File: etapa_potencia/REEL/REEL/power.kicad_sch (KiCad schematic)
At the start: 20 parts

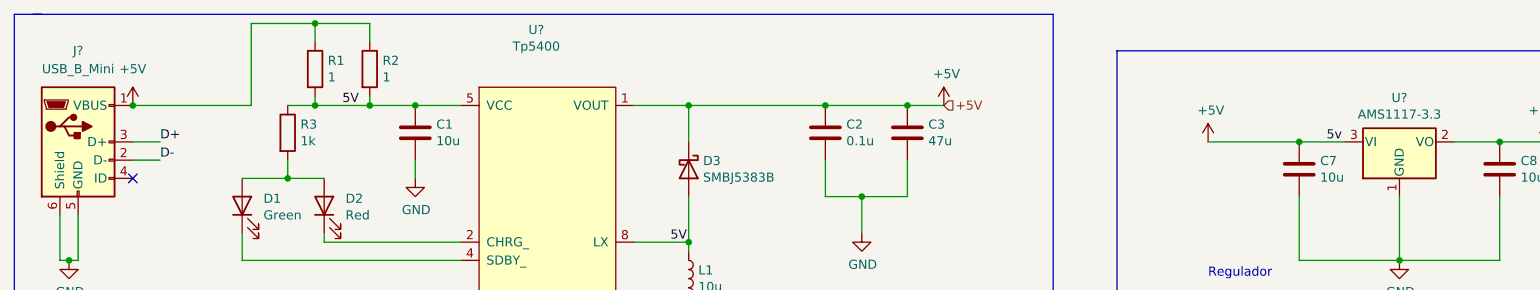
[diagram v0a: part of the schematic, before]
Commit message: Conexiones corregidas, PCB ordenada
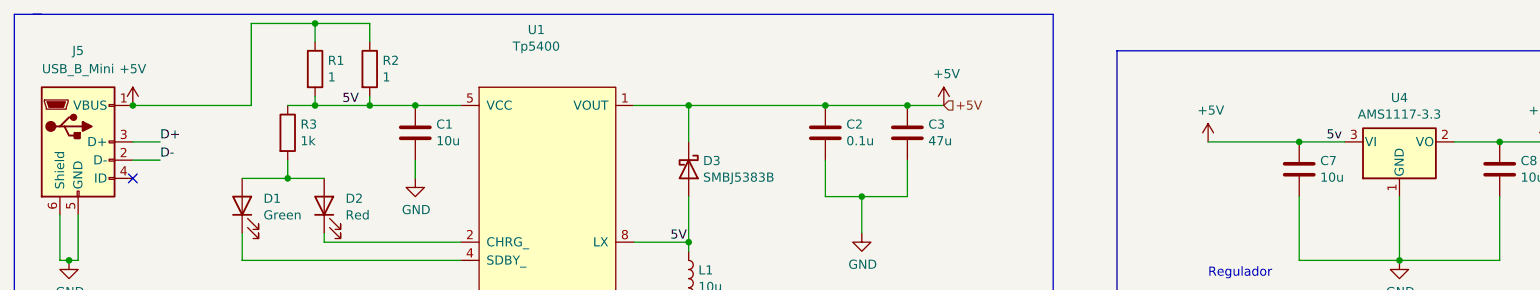
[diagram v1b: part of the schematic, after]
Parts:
- gave numbers to parts that had none: 3
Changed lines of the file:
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@@
   (symbol (lib_id "power:GND") (at 170.18 91.44 0) (unit 1)
     (in_bom yes) (on_board yes)
-    (property "Reference" "#PWR?" (id 0) (at 170.18 97.79 0)
+    (property "Reference" "#PWR024" (id 0) (at 170.18 97.79 0)
       (effects (font (size 1.27 1.27)) hide)
     )
@@
   (symbol (lib_id "Connector:USB_B_Mini") (at 60.96 78.74 0) (unit 1)
     (in_bom yes) (on_board yes) (fields_autoplaced)
-    (property "Reference" "J?" (id 0) (at 60.96 66.04 0))
+    (property "Reference" "J5" (id 0) (at 60.96 66.04 0))
     (property "Value" "USB_B_Mini" (id 1) (at 60.96 68.58 0))
     (property "Footprint" "Connector_USB:USB_Mini-B_AdamTech_MUSB-B5-S-VT-TSMT-1_SMD_Vertical" (id 2) (at 64.77 80.01 0)
@@
   (symbol (lib_id "power:GND") (at 245.11 95.25 0) (unit 1)
     (in_bom yes) (on_board yes)
-    (property "Reference" "#PWR?" (id 0) (at 245.11 101.6 0)
+    (property "Reference" "#PWR027" (id 0) (at 245.11 101.6 0)
       (effects (font (size 1.27 1.27)) hide)
     )
@@
   (symbol (lib_id "TP5400:Tp5400") (at 127 87.63 0) (unit 1)
     (in_bom yes) (on_board yes)
-    (property "Reference" "U?" (id 0) (at 124.8156 63.119 0))
+    (property "Reference" "U1" (id 0) (at 124.8156 63.119 0))
     (property "Value" "Tp5400" (id 1) (at 124.8156 65.4304 0))
     (property "Footprint" "KiCad:TP5410" (id 2) (at 121.92 68.58 0)
@@
   (symbol (lib_id "power:GND") (at 107.95 83.82 0) (unit 1)
     (in_bom yes) (on_board yes)
-    (property "Reference" "#PWR?" (id 0) (at 107.95 90.17 0)
+    (property "Reference" "#PWR022" (id 0) (at 107.95 90.17 0)
       (effects (font (size 1.27 1.27)) hide)
     )
@@
   (symbol (lib_id "Regulator_Linear:AMS1117-3.3") (at 245.11 78.74 0) (unit 1)
     (in_bom yes) (on_board yes)
-    (property "Reference" "U?" (id 0) (at 245.11 72.5932 0))
+    (property "Reference" "U4" (id 0) (at 245.11 72.5932 0))
     (property "Value" "AMS1117-3.3" (id 1) (at 245.11 74.9046 0))
     (property "Footprint" "Package_TO_SOT_SMD:SOT-223-3_TabPin2" (id 2) (at 245.11 73.66 0)
@@
   (symbol (lib_id "power:+3.3V") (at 265.43 78.74 0) (unit 1)
     (in_bom yes) (on_board yes)
-    (property "Reference" "#PWR?" (id 0) (at 265.43 82.55 0)
+    (property "Reference" "#PWR028" (id 0) (at 265.43 82.55 0)
       (effects (font (size 1.27 1.27)) hide)
     )
@@
   (symbol (lib_id "power:GND") (at 59.69 95.25 0) (unit 1)
     (in_bom yes) (on_board yes)
-    (property "Reference" "#PWR?" (id 0) (at 59.69 101.6 0)
+    (property "Reference" "#PWR020" (id 0) (at 59.69 101.6 0)
       (effects (font (size 1.27 1.27)) hide)
     )
@@
   (symbol (lib_id "power:GND") (at 138.43 129.54 0) (unit 1)
     (in_bom yes) (on_board yes)
-    (property "Reference" "#PWR?" (id 0) (at 138.43 135.89 0)
+    (property "Reference" "#PWR023" (id 0) (at 138.43 135.89 0)
       (effects (font (size 1.27 1.27)) hide)
     )
@@
   (symbol (lib_id "power:+5V") (at 218.44 78.74 0) (unit 1)
     (in_bom yes) (on_board yes)
-    (property "Reference" "#PWR?" (id 0) (at 218.44 82.55 0)
+    (property "Reference" "#PWR026" (id 0) (at 218.44 82.55 0)
       (effects (font (size 1.27 1.27)) hide)
     )
@@
   (symbol (lib_id "power:+5V") (at 181.61 73.66 0) (unit 1)
     (in_bom yes) (on_board yes)
-    (property "Reference" "#PWR?" (id 0) (at 181.61 77.47 0)
+    (property "Reference" "#PWR025" (id 0) (at 181.61 77.47 0)
       (effects (font (size 1.27 1.27)) hide)
     )
@@
   (symbol (lib_id "power:+5V") (at 68.58 73.66 0) (unit 1)
     (in_bom yes) (on_board yes) (fields_autoplaced)
-    (property "Reference" "#PWR?" (id 0) (at 68.58 77.47 0)
-      (effects (font (size 1.27 1.27)) hide)
-    )
+    (property "Reference" "#PWR021" (id 0) (at 68.58 77.47 0)
+      (effects (font (size 1.27 1.27)) hide)
+    )

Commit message: Primera organización huellas
Organización de huellas y conectores, falta parte de potencia
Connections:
- net +5V: no longer J5.1 (VBUS), R1.1, R2.1
- net +3V3 renamed +3.3V
- new net 5V_USB: J5.1 (VBUS), R1.1, R2.1
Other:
- moved on the sheet: C7, C8
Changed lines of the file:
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@@
   (junction (at 93.98 73.66) (diameter 0) (color 0 0 0 0)
-  )
-  (junction (at 68.58 73.66) (diameter 0) (color 0 0 0 0)
   )
   (junction (at 259.08 78.74) (diameter 0) (color 0 0 0 0)
@@
     (stroke (width 0) (type default) (color 0 0 0 0))
   )
-  (wire (pts (xy 231.14 95.25) (xy 231.14 86.36))
+  (wire (pts (xy 231.14 95.25) (xy 231.14 88.9))
     (stroke (width 0) (type default) (color 0 0 0 0))
   )
@@
     (stroke (width 0) (type default) (color 0 0 0 0))
   )
+  (wire (pts (xy 259.08 80.01) (xy 259.08 78.74))
+    (stroke (width 0) (type default) (color 0 0 0 0))
+  )
   (wire (pts (xy 93.98 62.23) (xy 93.98 64.77))
     (stroke (width 0) (type default) (color 0 0 0 0))
@@
     (stroke (width 0) (type default) (color 0 0 0 0))
   )
-  (wire (pts (xy 259.08 86.36) (xy 259.08 95.25))
+  (wire (pts (xy 259.08 87.63) (xy 259.08 95.25))
     (stroke (width 0) (type default) (color 0 0 0 0))
   )
@@
     (stroke (width 0) (type default) (color 0 0 0 0))
   )
+  (wire (pts (xy 231.14 81.28) (xy 231.14 78.74))
+    (stroke (width 0) (type default) (color 0 0 0 0))
+  )
   (wire (pts (xy 85.09 62.23) (xy 93.98 62.23))
     (stroke (width 0) (type default) (color 0 0 0 0))
@@
   )
   (label "5v" (at 234.95 78.74 0)
+    (effects (font (size 1.27 1.27)) (justify left bottom))
+  )
+  (label "5V_USB" (at 74.93 73.66 0)
     (effects (font (size 1.27 1.27)) (justify left bottom))
   )
@@
     (pin "1")
   )
-  (symbol (lib_id "Device:C") (at 231.14 82.55 0) (unit 1)
-    (in_bom yes) (on_board yes)
-    (property "Reference" "C7" (id 0) (at 234.061 81.3816 0)
-      (effects (font (size 1.27 1.27)) (justify left))
-    )
-    (property "Value" "10u" (id 1) (at 234.061 83.693 0)
-      (effects (font (size 1.27 1.27)) (justify left))
-    )
-    (property "Footprint" "Capacitor_SMD:C_1210_3225Metric_Pad1.33x2.70mm_HandSolder" (id 2) (at 232.1052 86.36 0)
-      (effects (font (size 1.27 1.27)) hide)
-    )
-    (property "Datasheet" "~" (id 3) (at 231.14 82.55 0)
+  (symbol (lib_id "Device:C") (at 231.14 85.09 0) (unit 1)
+    (in_bom yes) (on_board yes)
+    (property "Reference" "C7" (id 0) (at 234.061 83.9216 0)
+      (effects (font (size 1.27 1.27)) (justify left))
+    )
+    (property "Value" "10u" (id 1) (at 234.061 86.233 0)
+      (effects (font (size 1.27 1.27)) (justify left))
+    )
+    (property "Footprint" "Capacitor_SMD:C_1210_3225Metric_Pad1.33x2.70mm_HandSolder" (id 2) (at 232.1052 88.9 0)
+      (effects (font (size 1.27 1.27)) hide)
+    )
+    (property "Datasheet" "~" (id 3) (at 231.14 85.09 0)
       (effects (font (size 1.27 1.27)) hide)
     )
@@
     (pin "3")
   )
-  (symbol (lib_id "power:+3.3V") (at 265.43 78.74 0) (unit 1)
-    (in_bom yes) (on_board yes)
-    (property "Reference" "#PWR028" (id 0) (at 265.43 82.55 0)
-      (effects (font (size 1.27 1.27)) hide)
-    )
-    (property "Value" "+3.3V" (id 1) (at 265.811 74.3458 0))
-    (property "Footprint" "" (id 2) (at 265.43 78.74 0)
-      (effects (font (size 1.27 1.27)) hide)
-    )
-    (property "Datasheet" "" (id 3) (at 265.43 78.74 0)
-      (effects (font (size 1.27 1.27)) hide)
-    )
-    (pin "1")
-  )
   (symbol (lib_id "Device:LED") (at 95.25 87.63 90) (unit 1)
     (in_bom yes) (on_board yes)
@@
     (pin "2")
   )
-  (symbol (lib_id "Device:C") (at 259.08 82.55 0) (unit 1)
-    (in_bom yes) (on_board yes)
-    (property "Reference" "C8" (id 0) (at 262.001 81.3816 0)
-      (effects (font (size 1.27 1.27)) (justify left))
-    )
-    (property "Value" "10u" (id 1) (at 262.001 83.693 0)
-      (effects (font (size 1.27 1.27)) (justify left))
-    )
-    (property "Footprint" "Capacitor_SMD:C_1210_3225Metric_Pad1.33x2.70mm_HandSolder" (id 2) (at 260.0452 86.36 0)
-      (effects (font (size 1.27 1.27)) hide)
-    )
-    (property "Datasheet" "~" (id 3) (at 259.08 82.55 0)
+  (symbol (lib_id "Device:C") (at 259.08 83.82 0) (unit 1)
+    (in_bom yes) (on_board yes)
+    (property "Reference" "C8" (id 0) (at 262.001 82.6516 0)
+      (effects (font (size 1.27 1.27)) (justify left))
+    )
+    (property "Value" "10u" (id 1) (at 262.001 84.963 0)
+      (effects (font (size 1.27 1.27)) (justify left))
+    )
+    (property "Footprint" "Capacitor_SMD:C_1210_3225Metric_Pad1.33x2.70mm_HandSolder" (id 2) (at 260.0452 87.63 0)
+      (effects (font (size 1.27 1.27)) hide)
+    )
+    (property "Datasheet" "~" (id 3) (at 259.08 83.82 0)
       (effects (font (size 1.27 1.27)) hide)
     )
@@
     (pin "2")
   )
-  (symbol (lib_id "power:+5V") (at 181.61 73.66 0) (unit 1)
-    (in_bom yes) (on_board yes)
-    (property "Reference" "#PWR025" (id 0) (at 181.61 77.47 0)
-      (effects (font (size 1.27 1.27)) hide)
-    )
-    (property "Value" "+5V" (id 1) (at 181.991 69.2658 0))
-    (property "Footprint" "" (id 2) (at 181.61 73.66 0)
-      (effects (font (size 1.27 1.27)) hide)
-    )
-    (property "Datasheet" "" (id 3) (at 181.61 73.66 0)
-      (effects (font (size 1.27 1.27)) hide)
-    )
-    (pin "1")
-  )
-  (symbol (lib_id "power:+5V") (at 68.58 73.66 0) (unit 1)
-    (in_bom yes) (on_board yes) (fields_autoplaced)
-    (property "Reference" "#PWR021" (id 0) (at 68.58 77.47 0)
-      (effects (font (size 1.27 1.27)) hide)
-    )
-    (property "Value" "+5V" (id 1) (at 68.58 68.58 0))
-    (property "Footprint" "" (id 2) (at 68.58 73.66 0)
-      (effects (font (size 1.27 1.27)) hide)
-    )
-    (property "Datasheet" "" (id 3) (at 68.58 73.66 0)
-      (effects (font (size 1.27 1.27)) hide)
-    )
-    (pin "1")
-  )
   (symbol (lib_id "Device:C") (at 165.1 77.47 0) (unit 1)

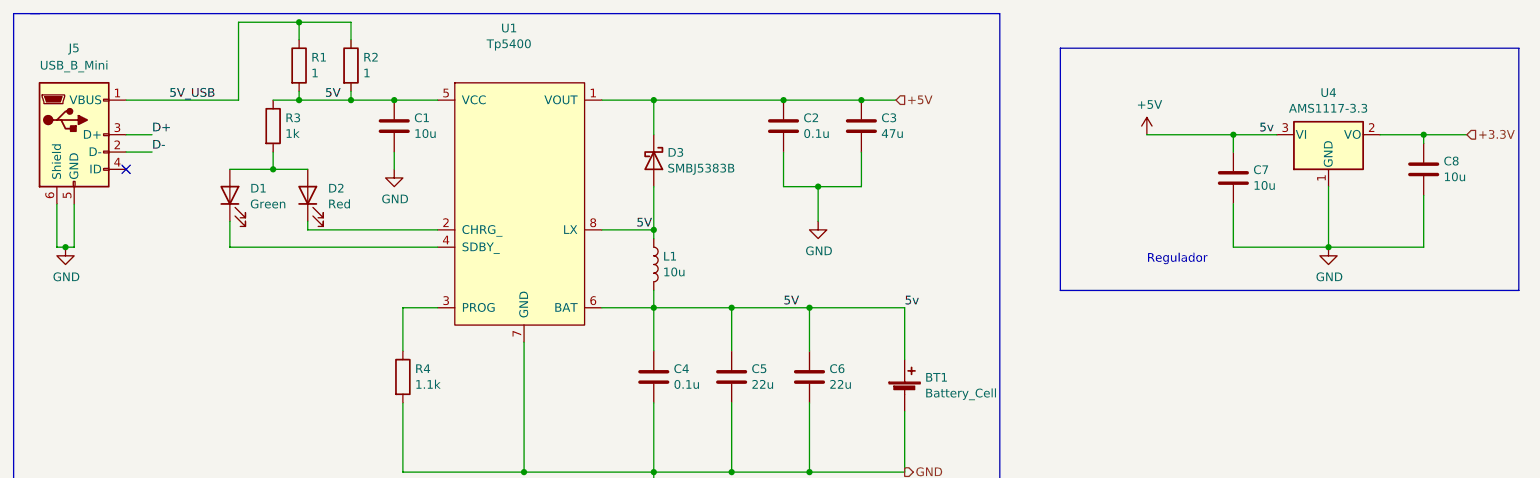
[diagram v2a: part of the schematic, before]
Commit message: Cambios en diagrama, separacion tierras, y capacitores
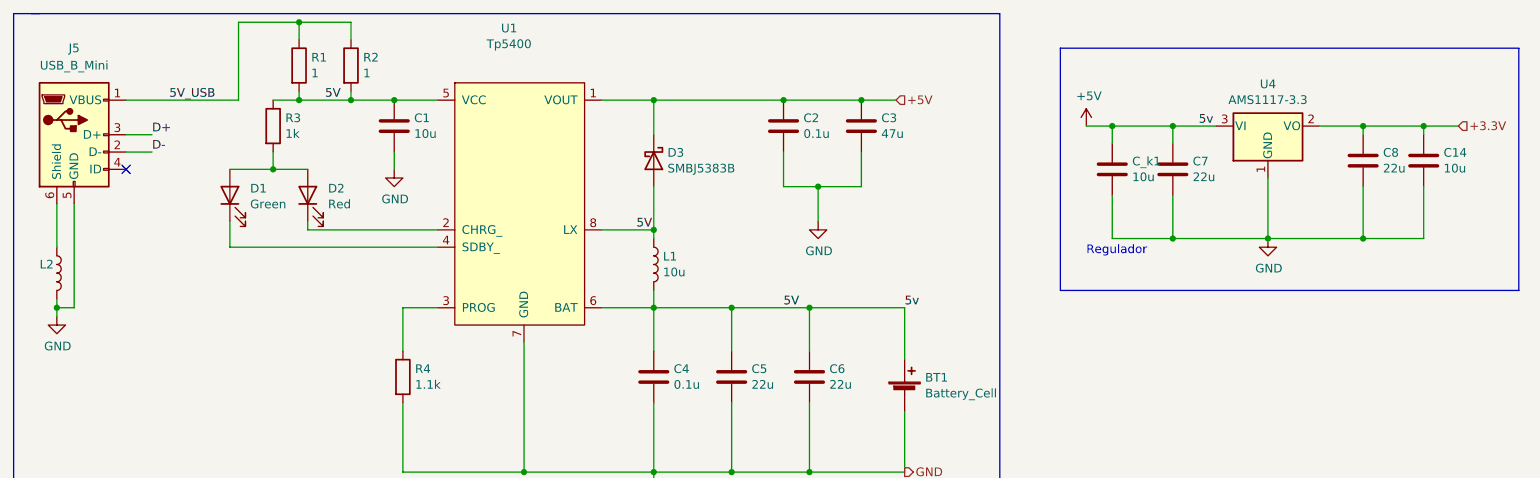
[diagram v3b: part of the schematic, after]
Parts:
- added C14, C_k1: 10u, Capacitor_SMD:C_1210_3225Metric_Pad1.33x2.70mm_HandSolder, symbol Device:C
- added L2: (no value), Inductor_SMD:L_6.3x6.3_H3, symbol Device:L
- BT1: footprint Battery:BatteryHolder_Bulgin_BX0036_1xC -> Connector_JST:JST_PH_B2B-PH-K_1x02_P2.00mm_Vertical
- C7, C8: value 10u -> 22u
- L1: footprint Inductor_SMD:L_0805_2012Metric_Pad1.05x1.20mm_HandSolder -> Inductor_SMD:L_6.3x6.3_H3
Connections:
- net +3.3V: now also C14.1
- net +5V: now also C_k1.1
- net GND: now also C14.2, C_k1.2, L2.2; no longer J5.6 (Shield)
- new net: J5.6 (Shield), L2.1
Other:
- moved on the sheet: C7, C8, U4

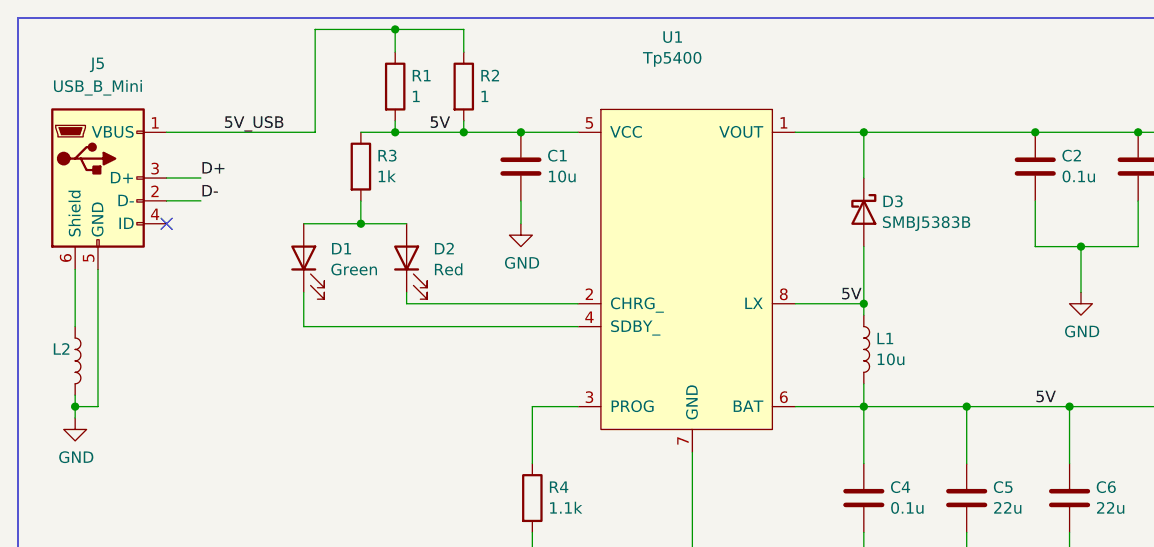
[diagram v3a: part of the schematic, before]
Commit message: modificaciones por caras
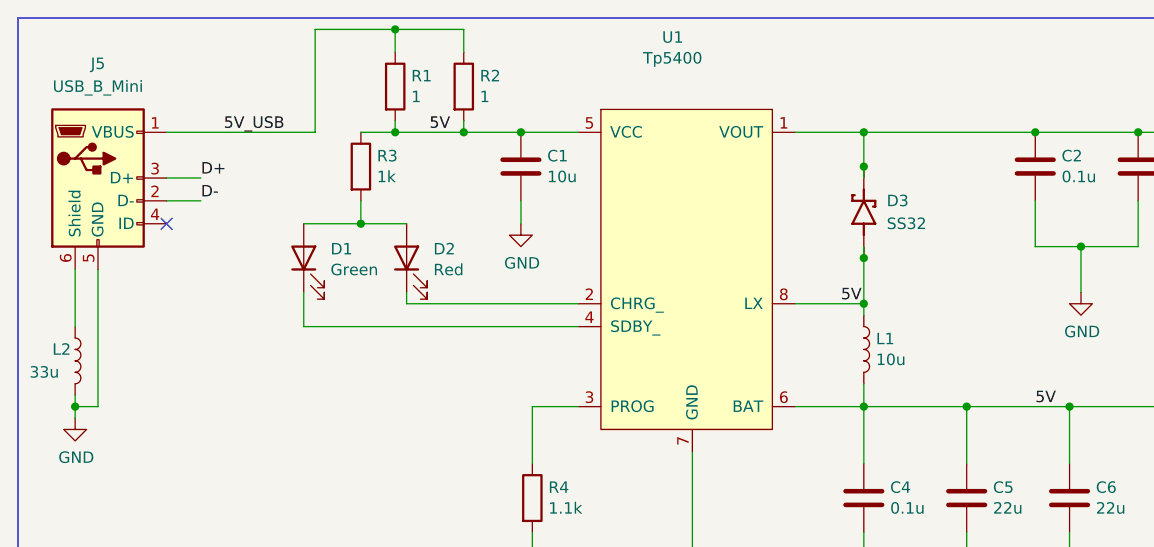
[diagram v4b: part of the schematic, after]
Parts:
- removed D3: SMBJ5383B, SMBJ5383B:SMBJ5383B, symbol Device:D_Schottky
- added D3: SS32, SS32:SS32, symbol SS32:SS32
- L2: value (none) -> 33u
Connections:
- net +5V: now also D3.A, D3.C
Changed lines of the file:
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@@
   (junction (at 101.6 73.66) (diameter 0) (color 0 0 0 0)
   )
+  (junction (at 146.05 77.47) (diameter 0) (color 0 0 0 0)
+  )
   (junction (at 259.08 77.47) (diameter 0) (color 0 0 0 0)
   )
@@
   )
   (junction (at 168.91 104.14) (diameter 0) (color 0 0 0 0)
+  )
+  (junction (at 146.05 87.63) (diameter 0) (color 0 0 0 0)
   )
   (junction (at 165.1 73.66) (diameter 0) (color 0 0 0 0)
@@
     (stroke (width 0) (type default) (color 0 0 0 0))
   )
+  (wire (pts (xy 146.05 87.63) (xy 146.05 86.36))
+    (stroke (width 0) (type default) (color 0 0 0 0))
+  )
   (wire (pts (xy 68.58 78.74) (xy 72.39 78.74))
     (stroke (width 0) (type default) (color 0 0 0 0))
@@
     (stroke (width 0) (type default) (color 0 0 0 0))
   )
+  (wire (pts (xy 146.05 77.47) (xy 146.05 78.74))
+    (stroke (width 0) (type default) (color 0 0 0 0))
+  )
   (wire (pts (xy 146.05 118.11) (xy 146.05 128.27))
     (stroke (width 0) (type default) (color 0 0 0 0))
@@
     (stroke (width 0) (type default) (color 0 0 0 0))
   )
-  (wire (pts (xy 146.05 73.66) (xy 146.05 78.74))
+  (wire (pts (xy 146.05 73.66) (xy 146.05 77.47))
     (stroke (width 0) (type default) (color 0 0 0 0))
   )
@@
     (stroke (width 0) (type default) (color 0 0 0 0))
   )
-  (wire (pts (xy 146.05 92.71) (xy 146.05 86.36))
+  (wire (pts (xy 146.05 92.71) (xy 146.05 87.63))
     (stroke (width 0) (type default) (color 0 0 0 0))
   )
@@
       (effects (font (size 1.27 1.27)) (justify left))
     )
-    (property "Value" "" (id 1) (at 53.34 100.33 0)
+    (property "Value" "33u" (id 1) (at 53.34 100.33 0)
       (effects (font (size 1.27 1.27)) (justify left))
     )
@@
     (pin "2")
   )
+  (symbol (lib_id "SS32:SS32") (at 146.05 82.55 90) (unit 1)
+    (in_bom yes) (on_board yes) (fields_autoplaced)
+    (property "Reference" "D3" (id 0) (at 148.59 81.2799 90)
+      (effects (font (size 1.27 1.27)) (justify right))
+    )
+    (property "Value" "SS32" (id 1) (at 148.59 83.8199 90)
+      (effects (font (size 1.27 1.27)) (justify right))
+    )
+    (property "Footprint" "SS32:SS32" (id 2) (at 146.05 82.55 0)
+      (effects (font (size 1.27 1.27)) (justify left bottom) hide)
+    )
+    (property "Datasheet" "" (id 3) (at 146.05 82.55 0)
+      (effects (font (size 1.27 1.27)) (justify left bottom) hide)
+    )
+    (property "MAXIMUM_PACKAGE_HEIGHT" "2.62 mm" (id 4) (at 146.05 82.55 0)
+      (effects (font (size 1.27 1.27)) (justify left bottom) hide)
+    )
+    (property "PARTREV" "Q2102" (id 5) (at 146.05 82.55 0)
+      (effects (font (size 1.27 1.27)) (justify left bottom) hide)
+    )
+    (property "STANDARD" "IPC-7351B" (id 6) (at 146.05 82.55 0)
+      (effects (font (size 1.27 1.27)) (justify left bottom) hide)
+    )
+    (property "MANUFACTURER" "Taiwan Semiconductor" (id 7) (at 146.05 82.55 0)
+      (effects (font (size 1.27 1.27)) (justify left bottom) hide)
+    )
+    (pin "A")
+    (pin "C")
+  )
   (symbol (lib_id "Device:C") (at 259.08 82.55 0) (unit 1)
     (in_bom yes) (on_board yes)
@@
       (effects (font (size 1.27 1.27)) hide)
     )
-    (pin "1")
-    (pin "2")
-  )
-  (symbol (lib_id "Device:D_Schottky") (at 146.05 82.55 270) (unit 1)
-    (in_bom yes) (on_board yes)
-    (property "Reference" "D3" (id 0) (at 148.0566 81.3816 90)
-      (effects (font (size 1.27 1.27)) (justify left))
-    )
-    (property "Value" "SMBJ5383B" (id 1) (at 148.0566 83.693 90)
-      (effects (font (size 1.27 1.27)) (justify left))
-    )
-    (property "Footprint" "SMBJ5383B:SMBJ5383B" (id 2) (at 146.05 82.55 0)
-      (effects (font (size 1.27 1.27)) hide)
-    )
-    (property "Datasheet" "~" (id 3) (at 146.05 82.55 0)
-      (effects (font (size 1.27 1.27)) hide)
-    )
